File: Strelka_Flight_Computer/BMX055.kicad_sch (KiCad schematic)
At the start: 4 parts, among them U11 BMX055

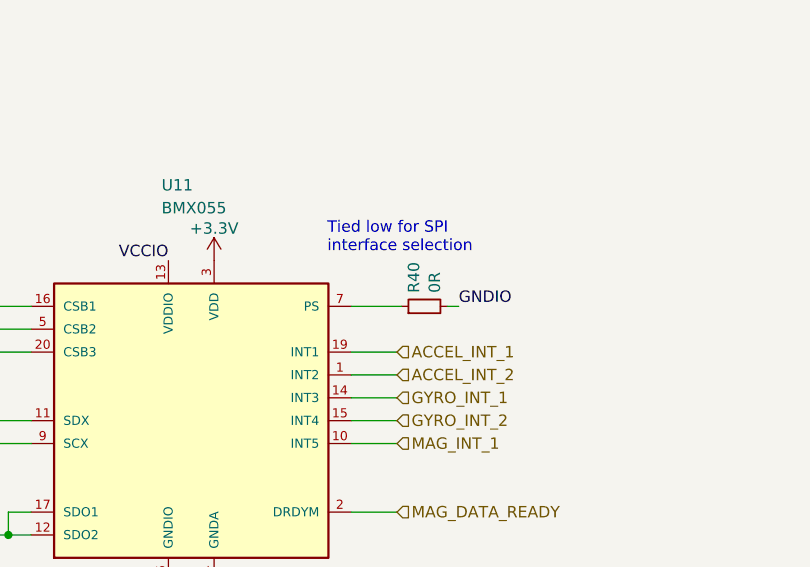
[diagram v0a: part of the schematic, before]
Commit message: Changed design rules
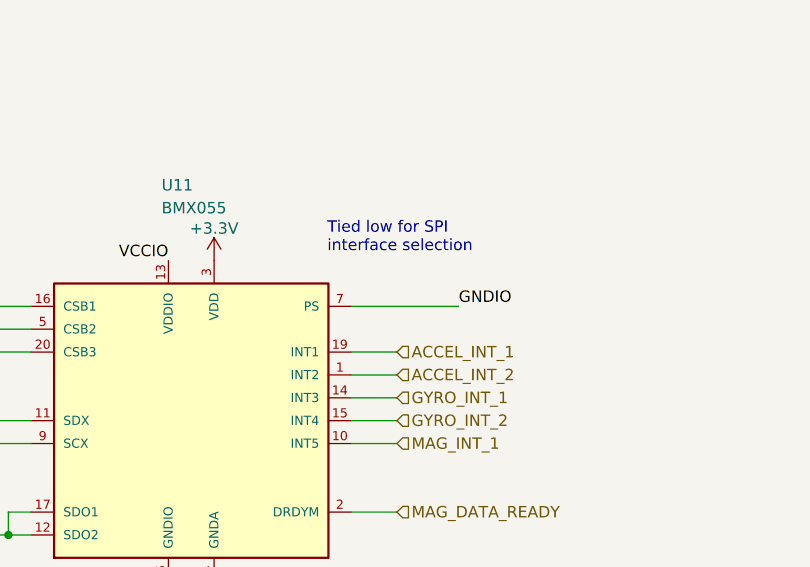
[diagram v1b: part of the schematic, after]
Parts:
- removed R40: 0R, Resistor_SMD:R_0603_1608Metric, symbol Device:R_Small
- C28, C29: footprint Capacitor_SMD:C_0603_1608Metric -> Capacitor_SMD:C_0402_1005Metric
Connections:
- net GND: now also U11.7 (PS)
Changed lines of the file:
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@@
-    (stroke (width 0) (type default))
-  )
-  (wire (pts (xy 179.07 80.772) (xy 180.34 80.772))
     (stroke (width 0) (type default))
   )
@@
     (stroke (width 0) (type default))
   )
-  (wire (pts (xy 168.402 80.772) (xy 173.99 80.772))
+  (wire (pts (xy 168.402 80.772) (xy 180.34 80.772))
     (stroke (width 0) (type default))
   )
@@
         (path "/e63e39d7-6ac0-4ffd-8aa3-1841a4541b55/78f71895-bddb-4f64-a608-99074f2d1c44/256d0f41-abcb-432e-a4cc-bcef1aa15bc3"
           (reference "#PWR0176") (unit 1)
-        )
-      )
-    )
-  )
-  (symbol (lib_id "Device:R_Small") (at 176.53 80.772 90) (unit 1)
-    (in_bom yes) (on_board yes) (dnp no)
-    (property "Reference" "R40" (at 175.3616 79.2734 0)
-      (effects (font (size 1.27 1.27)) (justify left))
-    )
-    (property "Value" "0R" (at 177.673 79.2734 0)
-      (effects (font (size 1.27 1.27)) (justify left))
-    )
-    (property "Footprint" "Resistor_SMD:R_0603_1608Metric" (at 176.53 80.772 0)
-      (effects (font (size 1.27 1.27)) hide)
-    )
-    (property "Datasheet" "~" (at 176.53 80.772 0)
-      (effects (font (size 1.27 1.27)) hide)
-    )
-    (pin "1")
-    (pin "2")
-    (instances
-      (project "Strelka_Flight_Computer"
-        (path "/e63e39d7-6ac0-4ffd-8aa3-1841a4541b55/78f71895-bddb-4f64-a608-99074f2d1c44/256d0f41-abcb-432e-a4cc-bcef1aa15bc3"
-          (reference "R40") (unit 1)
         )
       )
@@
       (effects (font (size 1.27 1.27)) (justify left))
     )
-    (property "Footprint" "Capacitor_SMD:C_0603_1608Metric" (at 165.862 120.142 0)
+    (property "Footprint" "Capacitor_SMD:C_0402_1005Metric" (at 165.862 120.142 0)
       (effects (font (size 1.27 1.27)) hide)
     )
@@
       (effects (font (size 1.27 1.27)) (justify left))
     )
-    (property "Footprint" "Capacitor_SMD:C_0603_1608Metric" (at 179.832 120.142 0)
-      (effects (font (size 1.27 1.27)) hide)
-    )
+    (property "Footprint" "Capacitor_SMD:C_0402_1005Metric" (at 179.832 120.142 0)
+      (effects (font (size 1.27 1.27)) hide)
+    )

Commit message: Continued routing
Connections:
- net +3V3 renamed +3.3V
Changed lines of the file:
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@@
     (effects (font (size 1.27 1.27)) (justify left))
   )
-  (symbol (lib_id "power:+3.3V") (at 153.162 75.692 0) (unit 1)
+  (symbol (lib_id "power:GND") (at 179.832 125.73 0) (unit 1)
+    (in_bom yes) (on_board yes) (dnp no)
+    (property "Reference" "#PWR0176" (at 179.832 132.08 0)
+      (effects (font (size 1.27 1.27)) hide)
+    )
+    (property "Value" "GND" (at 179.959 130.1242 0)
+      (effects (font (size 1.27 1.27)))
+    )
+    (property "Footprint" "" (at 179.832 125.73 0)
+      (effects (font (size 1.27 1.27)) hide)
+    )
+    (property "Datasheet" "" (at 179.832 125.73 0)
+      (effects (font (size 1.27 1.27)) hide)
+    )
+    (pin "1")
+    (instances
+      (project "Strelka_Flight_Computer"
+        (path "/e63e39d7-6ac0-4ffd-8aa3-1841a4541b55/78f71895-bddb-4f64-a608-99074f2d1c44/256d0f41-abcb-432e-a4cc-bcef1aa15bc3"
+          (reference "#PWR0176") (unit 1)
+        )
+      )
+    )
+  )
+  (symbol (lib_name "+3.3V_1") (lib_id "power:+3.3V") (at 179.832 115.57 0) (unit 1)
     (in_bom yes) (on_board yes) (dnp no) (fields_autoplaced)
-    (property "Reference" "#PWR0172" (at 153.162 79.502 0)
-      (effects (font (size 1.27 1.27)) hide)
-    )
-    (property "Value" "+3.3V" (at 153.162 72.1162 0)
-      (effects (font (size 1.27 1.27)))
-    )
-    (property "Footprint" "" (at 153.162 75.692 0)
-      (effects (font (size 1.27 1.27)) hide)
-    )
-    (property "Datasheet" "" (at 153.162 75.692 0)
-      (effects (font (size 1.27 1.27)) hide)
-    )
-    (pin "1")
-    (instances
-      (project "Strelka_Flight_Computer"
-        (path "/e63e39d7-6ac0-4ffd-8aa3-1841a4541b55/78f71895-bddb-4f64-a608-99074f2d1c44/256d0f41-abcb-432e-a4cc-bcef1aa15bc3"
-          (reference "#PWR0172") (unit 1)
-        )
-      )
-    )
-  )
-  (symbol (lib_id "power:GND") (at 179.832 125.73 0) (unit 1)
-    (in_bom yes) (on_board yes) (dnp no)
-    (property "Reference" "#PWR0176" (at 179.832 132.08 0)
-      (effects (font (size 1.27 1.27)) hide)
-    )
-    (property "Value" "GND" (at 179.959 130.1242 0)
-      (effects (font (size 1.27 1.27)))
-    )
-    (property "Footprint" "" (at 179.832 125.73 0)
-      (effects (font (size 1.27 1.27)) hide)
-    )
-    (property "Datasheet" "" (at 179.832 125.73 0)
-      (effects (font (size 1.27 1.27)) hide)
-    )
-    (pin "1")
-    (instances
-      (project "Strelka_Flight_Computer"
-        (path "/e63e39d7-6ac0-4ffd-8aa3-1841a4541b55/78f71895-bddb-4f64-a608-99074f2d1c44/256d0f41-abcb-432e-a4cc-bcef1aa15bc3"
-          (reference "#PWR0176") (unit 1)
+    (property "Reference" "#PWR07" (at 179.832 119.38 0)
+      (effects (font (size 1.27 1.27)) hide)
+    )
+    (property "Value" "+3.3V" (at 179.832 112.395 0)
+      (effects (font (size 1.27 1.27)))
+    )
+    (property "Footprint" "" (at 179.832 115.57 0)
+      (effects (font (size 1.27 1.27)) hide)
+    )
+    (property "Datasheet" "" (at 179.832 115.57 0)
+      (effects (font (size 1.27 1.27)) hide)
+    )
+    (pin "1")
+    (instances
+      (project "Strelka_Flight_Computer"
+        (path "/e63e39d7-6ac0-4ffd-8aa3-1841a4541b55/e94c6cea-6c6c-4b5f-a840-b97a15d9406a"
+          (reference "#PWR07") (unit 1)
+        )
+        (path "/e63e39d7-6ac0-4ffd-8aa3-1841a4541b55/78f71895-bddb-4f64-a608-99074f2d1c44/256d0f41-abcb-432e-a4cc-bcef1aa15bc3"
+          (reference "#PWR012") (unit 1)
         )
       )
@@
     )
   )
-  (symbol (lib_id "power:+3.3V") (at 179.832 115.57 0) (unit 1)
+  (symbol (lib_name "+3.3V_1") (lib_id "power:+3.3V") (at 153.162 75.692 0) (unit 1)
     (in_bom yes) (on_board yes) (dnp no) (fields_autoplaced)
-    (property "Reference" "#PWR0177" (at 179.832 119.38 0)
-      (effects (font (size 1.27 1.27)) hide)
-    )
-    (property "Value" "+3.3V" (at 179.832 111.9942 0)
-      (effects (font (size 1.27 1.27)))
-    )
-    (property "Footprint" "" (at 179.832 115.57 0)
-      (effects (font (size 1.27 1.27)) hide)
-    )
-    (property "Datasheet" "" (at 179.832 115.57 0)
-      (effects (font (size 1.27 1.27)) hide)
-    )
-    (pin "1")
-    (instances
-      (project "Strelka_Flight_Computer"
-        (path "/e63e39d7-6ac0-4ffd-8aa3-1841a4541b55/78f71895-bddb-4f64-a608-99074f2d1c44/256d0f41-abcb-432e-a4cc-bcef1aa15bc3"
-          (reference "#PWR0177") (unit 1)
-        )
-      )
-    )
-  )
-  (symbol (lib_id "power:+3.3V") (at 135.89 116.84 0) (unit 1)
+    (property "Reference" "#PWR07" (at 153.162 79.502 0)
+      (effects (font (size 1.27 1.27)) hide)
+    )
+    (property "Value" "+3.3V" (at 153.162 72.517 0)
+      (effects (font (size 1.27 1.27)))
+    )
+    (property "Footprint" "" (at 153.162 75.692 0)
+      (effects (font (size 1.27 1.27)) hide)
+    )
+    (property "Datasheet" "" (at 153.162 75.692 0)
+      (effects (font (size 1.27 1.27)) hide)
+    )
+    (pin "1")
+    (instances
+      (project "Strelka_Flight_Computer"
+        (path "/e63e39d7-6ac0-4ffd-8aa3-1841a4541b55/e94c6cea-6c6c-4b5f-a840-b97a15d9406a"
+          (reference "#PWR07") (unit 1)
+        )
+        (path "/e63e39d7-6ac0-4ffd-8aa3-1841a4541b55/78f71895-bddb-4f64-a608-99074f2d1c44/256d0f41-abcb-432e-a4cc-bcef1aa15bc3"
+          (reference "#PWR013") (unit 1)
+        )
+      )
+    )
+  )
+  (symbol (lib_name "+3.3V_1") (lib_id "power:+3.3V") (at 135.89 116.84 0) (unit 1)
     (in_bom yes) (on_board yes) (dnp no) (fields_autoplaced)
-    (property "Reference" "#PWR0175" (at 135.89 120.65 0)
-      (effects (font (size 1.27 1.27)) hide)
-    )
-    (property "Value" "+3.3V" (at 135.89 113.2642 0)
+    (property "Reference" "#PWR07" (at 135.89 120.65 0)
+      (effects (font (size 1.27 1.27)) hide)
+    )
+    (property "Value" "+3.3V" (at 135.89 113.665 0)
       (effects (font (size 1.27 1.27)))
     )
@@
     (instances
       (project "Strelka_Flight_Computer"
-        (path "/e63e39d7-6ac0-4ffd-8aa3-1841a4541b55/78f71895-bddb-4f64-a608-99074f2d1c44/256d0f41-abcb-432e-a4cc-bcef1aa15bc3"
-          (reference "#PWR0175") (unit 1)
-        )
-      )
+        (path "/e63e39d7-6ac0-4ffd-8aa3-1841a4541b55/e94c6cea-6c6c-4b5f-a840-b97a15d9406a"
+          (reference "#PWR07") (unit 1)
+        )
+        (path "/e63e39d7-6ac0-4ffd-8aa3-1841a4541b55/78f71895-bddb-4f64-a608-99074f2d1c44/256d0f41-abcb-432e-a4cc-bcef1aa15bc3"
+          (reference "#PWR011") (unit 1)
+        )
+      )

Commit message: Created BOM
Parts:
- C28, C29: value 100nF -> 100n
- U11: LCSC (none) -> C94022; LCSC# C94022 -> (none)
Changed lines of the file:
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@@
       (effects (font (size 1.27 1.27)) (justify left bottom) hide)
     )
-    (property "LCSC#" "C94022" (at 150.622 93.472 0)
+    (property "LCSC" "C94022" (at 150.622 93.472 0)
       (effects (font (size 1.27 1.27)) hide)
     )
@@
       (effects (font (size 1.27 1.27)) (justify left))
     )
-    (property "Value" "100nF" (at 168.402 120.142 0)
+    (property "Value" "100n" (at 168.402 120.142 0)
       (effects (font (size 1.27 1.27)) (justify left))
     )
@@
       (effects (font (size 1.27 1.27)) (justify left))
     )
-    (property "Value" "100nF" (at 182.372 120.142 0)
+    (property "Value" "100n" (at 182.372 120.142 0)
       (effects (font (size 1.27 1.27)) (justify left))
     )

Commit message: Added LCSC mpn to all relevent parts
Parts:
- C28, C29: LCSC (none) -> C1525
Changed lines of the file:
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@@
+      (effects (font (size 1.27 1.27)) hide)
+    )
+    (property "LCSC" " C1525" (at 165.862 120.142 0)
       (effects (font (size 1.27 1.27)) hide)
     )
@@
       (effects (font (size 1.27 1.27)) hide)
     )
+    (property "LCSC" " C1525" (at 179.832 120.142 0)
+      (effects (font (size 1.27 1.27)) hide)
+    )
